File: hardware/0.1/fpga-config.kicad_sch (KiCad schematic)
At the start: 34 parts, among them J2 JTAG, J5 USB_C_Receptacle_USB2.0, Q1 BSS138, SW1 KMR2, U1 ECP5U_12_CABGA256, U4 USBLC6-2P6, U6 W25Q128JVPIM

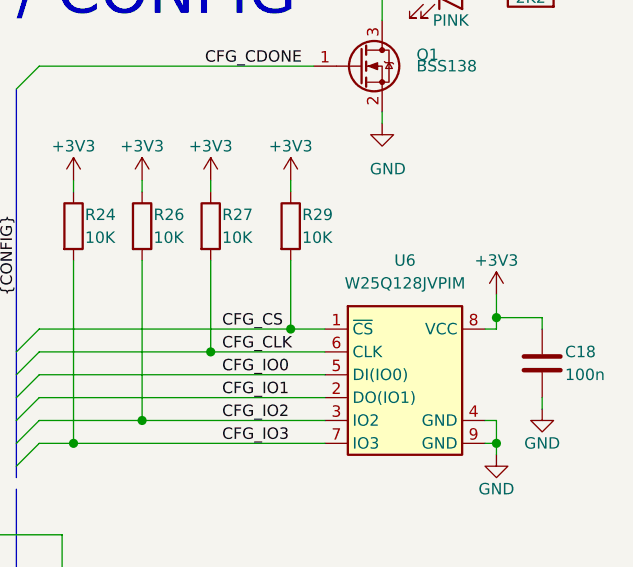
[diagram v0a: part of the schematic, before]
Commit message: set clearances to a more reasonable number
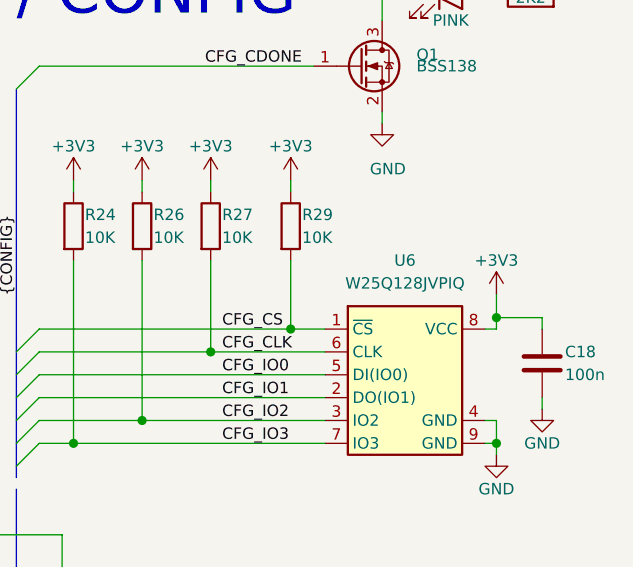
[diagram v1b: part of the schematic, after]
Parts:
- U6: value W25Q128JVPIM -> W25Q128JVPIQ; MPN W25Q128JVPIM -> W25Q128JVPIQ; Mouser 454-W25Q128JVPIM -> 454-W25Q128JVPIQ
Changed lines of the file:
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@@
-(kicad_sch (version 20200827) (generator eeschema)
+(kicad_sch (version 20200828) (generator eeschema)
   (page 3 5)
   (paper "A4")
@@
   (junction (at 269.24 57.15) (diameter 1.016) (color 0 0 0 0))
   (junction (at 269.24 71.12) (diameter 1.016) (color 0 0 0 0))
+  (no_connect (at 229.87 121.92))
+  (no_connect (at 229.87 111.76))
+  (no_connect (at 229.87 114.3))
+  (no_connect (at 46.355 66.04))
+  (no_connect (at 229.87 137.16))
+  (no_connect (at 229.87 144.78))
   (no_connect (at 229.87 116.84))
-  (no_connect (at 229.87 121.92))
   (no_connect (at 229.87 119.38))
-  (no_connect (at 229.87 114.3))
-  (no_connect (at 229.87 144.78))
-  (no_connect (at 229.87 137.16))
   (no_connect (at 46.355 63.5))
-  (no_connect (at 46.355 66.04))
-  (no_connect (at 229.87 111.76))
   (bus_entry (at 114.935 49.53) (size 2.54 -2.54)
     (stroke (width 0.1524) (type solid) (color 0 0 0 0))
@@
     (in_bom yes) (on_board yes)
     (property "Reference" "U6" (id 0) (at 259.08 50.8 0))
-    (property "Value" "W25Q128JVPIM" (id 1) (at 259.08 53.34 0))
+    (property "Value" "W25Q128JVPIQ" (id 1) (at 259.08 53.34 0))
     (property "Footprint" "josh-soic-sot-etc:WSON-8-1EP_6x5mm_P1.27mm_EP3.4x4.3mm" (id 2) (at 262.89 63.5 0)
       (effects (font (size 1.27 1.27)) hide)
@@
       (effects (font (size 1.27 1.27)) hide)
     )
-    (property "MPN" "W25Q128JVPIM" (id 4) (at 262.89 63.5 0)
+    (property "MPN" "W25Q128JVPIQ" (id 4) (at 262.89 63.5 0)
       (effects (font (size 1.27 1.27)) hide)
     )
@@
       (effects (font (size 1.27 1.27)) hide)
     )
-    (property "Mouser" "454-W25Q128JVPIM" (id 6) (at 262.89 63.5 0)
-      (effects (font (size 1.27 1.27)) hide)
-    )
+    (property "Mouser" "454-W25Q128JVPIQ" (id 6) (at 262.89 63.5 0)
+      (effects (font (size 1.27 1.27)) hide)
+    )

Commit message: update readme following r0.1 bringup
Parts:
- R20: DNP DNP -> (none)
- R21: value 2K2 -> 1K5; LCSC C25933 -> C25867; MPN 0402WGJ0222TCE -> 0402WGF1501TCE
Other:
- note removed: "Enables bootloader to reset into user land. DNP until bootloader development begins."
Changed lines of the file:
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@@
   (junction (at 269.24 71.12) (diameter 1.016) (color 0 0 0 0))
   (no_connect (at 229.87 121.92))
+  (no_connect (at 229.87 137.16))
+  (no_connect (at 229.87 111.76))
+  (no_connect (at 229.87 144.78))
+  (no_connect (at 46.355 63.5))
+  (no_connect (at 46.355 66.04))
+  (no_connect (at 229.87 114.3))
+  (no_connect (at 229.87 116.84))
   (no_connect (at 229.87 119.38))
-  (no_connect (at 229.87 137.16))
-  (no_connect (at 229.87 114.3))
-  (no_connect (at 46.355 66.04))
-  (no_connect (at 46.355 63.5))
-  (no_connect (at 229.87 116.84))
-  (no_connect (at 229.87 144.78))
-  (no_connect (at 229.87 111.76))
   (bus_entry (at 114.935 49.53) (size 2.54 -2.54)
     (stroke (width 0.1524) (type solid) (color 0 0 0 0))
@@
   )
   (text "CFG[2:0] = 010\nBoot from SPI Flash\n" (at 182.88 113.03 0)
-    (effects (font (size 1.27 1.27)) (justify left bottom))
-  )
-  (text "Enables bootloader to reset into user land.\nDNP until bootloader development begins."
-    (at 200.66 154.94 0)
     (effects (font (size 1.27 1.27)) (justify left bottom))
   )
@@
       (effects (font (size 1.27 1.27)) hide)
     )
-    (property "DNP" "DNP" (id 4) (at 212.09 144.78 90))
+    (property "DNP" "" (id 4) (at 212.09 144.78 90))
     (property "MPN" "0402WGJ0220TCE" (id 5) (at 212.09 142.24 0)
       (effects (font (size 1.27 1.27)) hide)
@@
     (in_bom yes) (on_board yes)
     (property "Reference" "R21" (id 0) (at 273.05 19.05 90))
-    (property "Value" "2K2" (id 1) (at 273.05 21.59 90))
+    (property "Value" "1K5" (id 1) (at 273.05 21.59 90))
     (property "Footprint" "Resistor_SMD:R_0402_1005Metric" (id 2) (at 273.05 23.368 90)
       (effects (font (size 1.27 1.27)) hide)
@@
       (effects (font (size 1.27 1.27)) hide)
     )
-    (property "LCSC" "C25933" (id 4) (at 273.05 21.59 0)
-      (effects (font (size 1.27 1.27)) hide)
-    )
-    (property "MPN" "0402WGJ0222TCE" (id 5) (at 273.05 21.59 0)
-      (effects (font (size 1.27 1.27)) hide)
-    )
+    (property "LCSC" "C25867" (id 4) (at 273.05 21.59 0)
+      (effects (font (size 1.27 1.27)) hide)
+    )
+    (property "MPN" "0402WGF1501TCE" (id 5) (at 273.05 21.59 0)
+      (effects (font (size 1.27 1.27)) hide)
+    )

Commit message: update BOM
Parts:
- D2: Notes (none) -> If not using exact PN, may want to increase resistor values
- F1: Mouser (none) -> 576-0603L100SLYR
- J2: now left out of the parts list
- J5: Notes (none) -> Digikey: USB4105-GF-A
- Q1: Mouser (none) -> 771-BSS138PW115
- SW1: Mouser (none) -> 611-KMR211G-LFS; Notes (none) -> Mouser actual C&K, LCSC compatiable PN
- U1: Manufacturer Lattice -> Lattice Semiconductor
- U4: Mouser (none) -> 511-USBLC6-2P6
- U6: LCSC (none) -> W25Q128JVPIQ
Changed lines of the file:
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@@
-(kicad_sch (version 20200828) (generator eeschema)
-  (page 3 5)
+(kicad_sch (version 20201015) (generator eeschema)
+  (page 1 5)
   (paper "A4")
   (bus_alias "CONFIG" (members "CFG_CLK" "CFG_IO[0..3]" "CFG_CDONE" "CFG_CS"))
@@
   (junction (at 269.24 57.15) (diameter 1.016) (color 0 0 0 0))
   (junction (at 269.24 71.12) (diameter 1.016) (color 0 0 0 0))
+  (no_connect (at 229.87 119.38))
   (no_connect (at 229.87 121.92))
+  (no_connect (at 46.355 66.04))
+  (no_connect (at 46.355 63.5))
+  (no_connect (at 229.87 116.84))
+  (no_connect (at 229.87 144.78))
   (no_connect (at 229.87 137.16))
+  (no_connect (at 229.87 114.3))
   (no_connect (at 229.87 111.76))
-  (no_connect (at 229.87 144.78))
-  (no_connect (at 46.355 63.5))
-  (no_connect (at 46.355 66.04))
-  (no_connect (at 229.87 114.3))
-  (no_connect (at 229.87 116.84))
-  (no_connect (at 229.87 119.38))
   (bus_entry (at 114.935 49.53) (size 2.54 -2.54)
     (stroke (width 0.1524) (type solid) (color 0 0 0 0))
@@
       (effects (font (size 1.27 1.27)) hide)
     )
+    (property "Mouser" "576-0603L100SLYR " (id 4) (at 75.565 35.56 0)
+      (effects (font (size 1.27 1.27)) hide)
+    )
   )
   (symbol (lib_id "Device:LED") (at 264.16 21.59 0) (unit 1)
@@
       (effects (font (size 1.27 1.27)) hide)
     )
+    (property "Notes" "If not using exact PN, may want to increase resistor values" (id 4) (at 264.16 21.59 0)
+      (effects (font (size 1.27 1.27)) hide)
+    )
   )
   (symbol (lib_id "Device:C") (at 53.975 30.48 90) (unit 1)
@@
       (effects (font (size 1.27 1.27)) hide)
     )
+    (property "Mouser" "611-KMR211G-LFS" (id 4) (at 160.02 140.97 0)
+      (effects (font (size 1.27 1.27)) hide)
+    )
+    (property "Notes" "Mouser actual C&K, LCSC compatiable PN" (id 5) (at 160.02 140.97 0)
+      (effects (font (size 1.27 1.27)) hide)
+    )
   )
   (symbol (lib_id "Connector:Conn_01x06_Male") (at 44.45 106.68 0) (mirror y) (unit 1)
-    (in_bom yes) (on_board yes)
+    (in_bom no) (on_board yes)
     (property "Reference" "J2" (id 0) (at 43.18 96.52 0)
       (effects (font (size 1.27 1.27)) (justify right))
@@
       (effects (font (size 1.27 1.27)) hide)
     )
+    (property "Mouser" "771-BSS138PW115 " (id 4) (at 254 29.21 0)
+      (effects (font (size 1.27 1.27)) hide)
+    )
   )
   (symbol (lib_name "josh-ic:ECP5U_12_CABGA256_1") (lib_id "josh-ic:ECP5U_12_CABGA256") (at 78.74 104.14 0) (unit 9)
@@
       (effects (font (size 1.524 1.524)) (justify right) hide)
     )
-    (property "Manufacturer" "Lattice" (id 5) (at 78.74 104.14 0)
+    (property "Manufacturer" "Lattice Semiconductor" (id 5) (at 78.74 104.14 0)
       (effects (font (size 1.27 1.27)) hide)
     )
@@
       (effects (font (size 1.27 1.27)) hide)
     )
+    (property "LCSC" "W25Q128JVPIQ" (id 4) (at 262.89 63.5 0)
+      (effects (font (size 1.27 1.27)) hide)
+    )
   )
   (symbol (lib_id "josh-ic:USBLC6-2SC6") (at 70.485 52.07 0) (unit 1)
@@
       (effects (font (size 1.27 1.27)) hide)
     )
+    (property "Mouser" "511-USBLC6-2P6" (id 4) (at 70.485 52.07 0)
+      (effects (font (size 1.27 1.27)) hide)
+    )
   )
   (symbol (lib_id "Connector:USB_C_Receptacle_USB2.0") (at 31.115 50.8 0) (unit 1)
@@
       (effects (font (size 1.27 1.27)) hide)
     )
+    (property "Notes" "Digikey: USB4105-GF-A" (id 4) (at 31.115 50.8 0)
+      (effects (font (size 1.27 1.27)) hide)
+    )
   )
   (symbol (lib_id "josh-ic:ECP5U_12_CABGA256") (at 251.46 132.08 0) (unit 8)
@@
       (effects (font (size 1.524 1.524)) (justify right) hide)
     )
-    (property "Manufacturer" "Lattice" (id 5) (at 251.46 132.08 0)
-      (effects (font (size 1.27 1.27)) hide)
-    )
+    (property "Manufacturer" "Lattice Semiconductor" (id 5) (at 251.46 132.08 0)
+      (effects (font (size 1.27 1.27)) hide)
+    )
